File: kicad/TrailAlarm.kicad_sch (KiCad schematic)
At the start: 34 parts

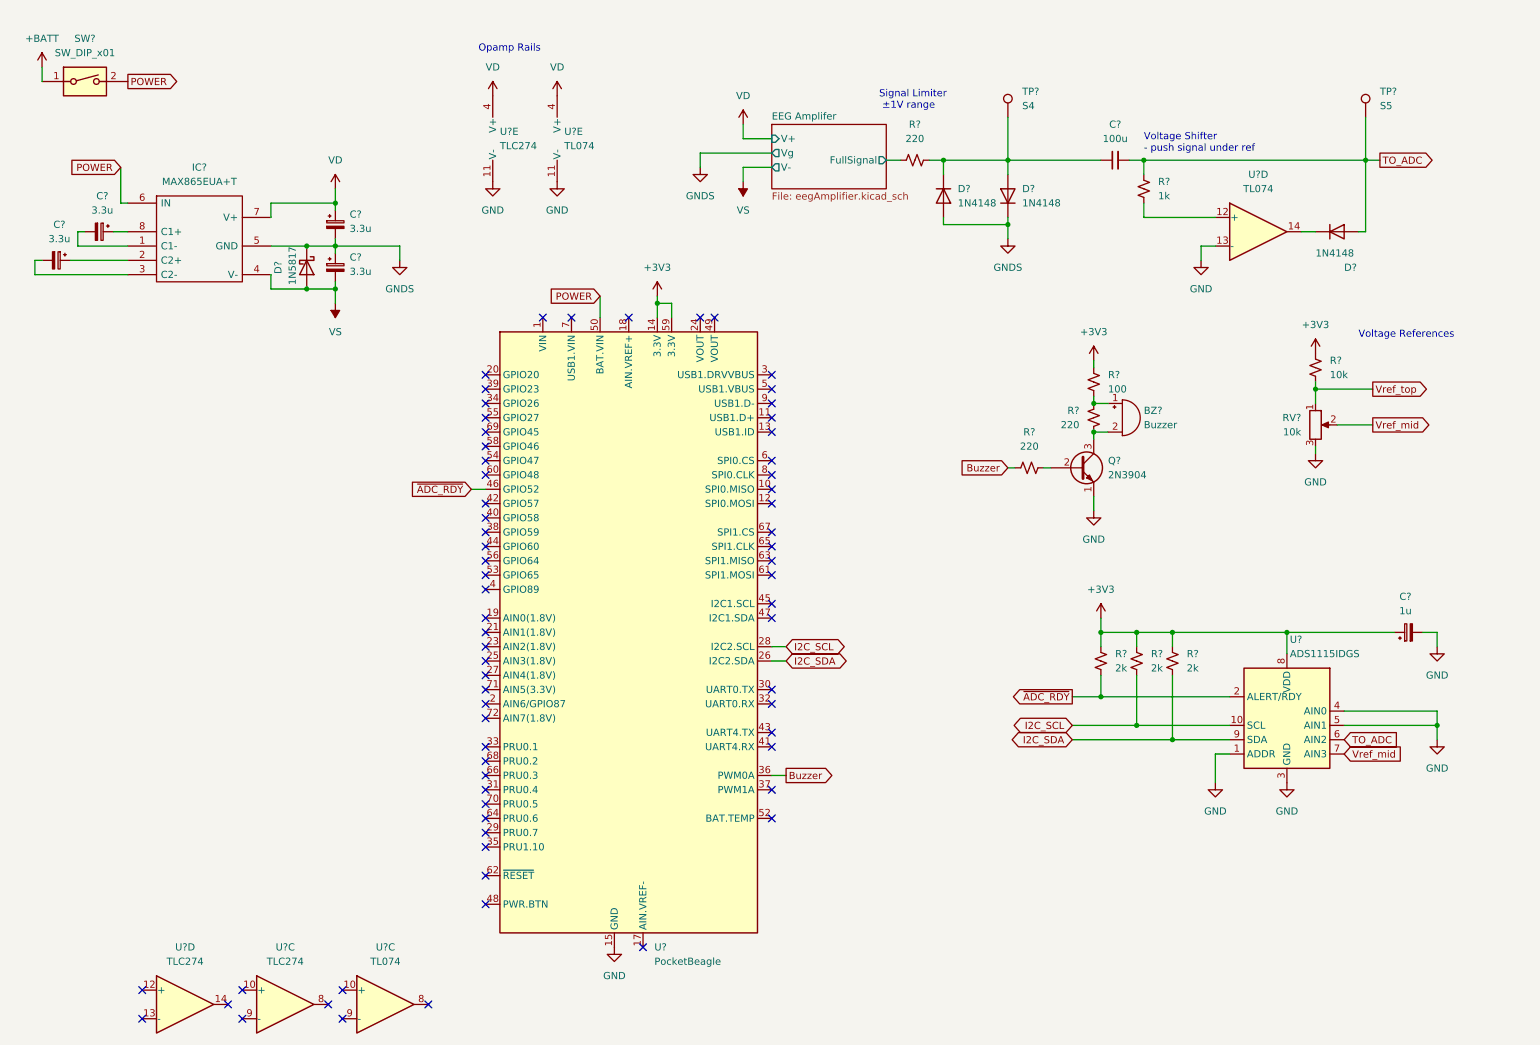
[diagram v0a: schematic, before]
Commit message: Add jumpers to power rails
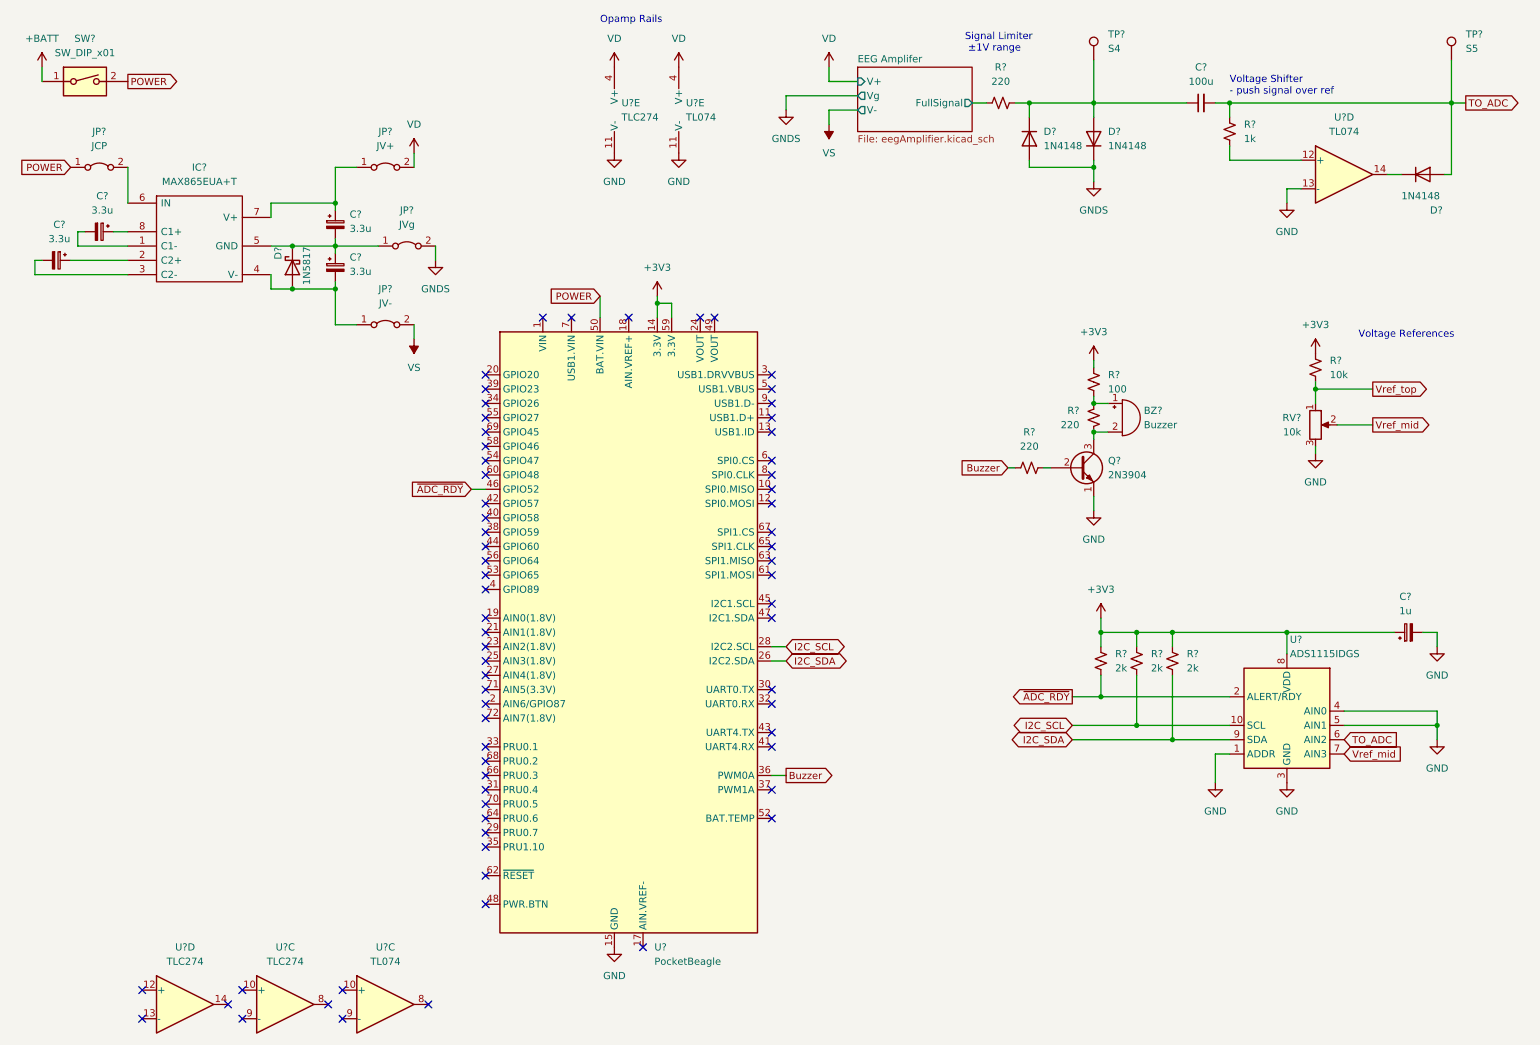
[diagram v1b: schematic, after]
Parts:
- added JP?: JV+, symbol Jumper:Jumper_2_Bridged
- added JP?: JCP, symbol Jumper:Jumper_2_Bridged
- added JP?: JVg, symbol Jumper:Jumper_2_Bridged
- added JP?: JV-, symbol Jumper:Jumper_2_Bridged
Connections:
- net GNDS: now also JP?.2 (B); no longer C?.1, C?.2, D?.1 (K), IC?.5 (GND)
- net POWER: now also JP?.1 (A); no longer IC?.6 (IN)
- net VD: now also JP?.2 (B); no longer C?.1, IC?.7 (V+)
- net VS: now also JP?.2 (B); no longer C?.2, D?.2 (A), IC?.4 (V-)
- new net: C?.1, C?.2, D?.1 (K), IC?.5 (GND), JP?.1 (A)
- new net: C?.2, D?.2 (A), IC?.4 (V-), JP?.1 (A)
- new net: C?.1, IC?.7 (V+), JP?.1 (A)
- new net: IC?.6 (IN), JP?.2 (B)
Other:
- note added: "Voltage Shifter - push signal over ref"
- note removed: "Voltage Shifter - push signal under ref"
- moved on the sheet: C?, D?, R?, TP?, U?D, U?E

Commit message: Pin assignment, electrode headers
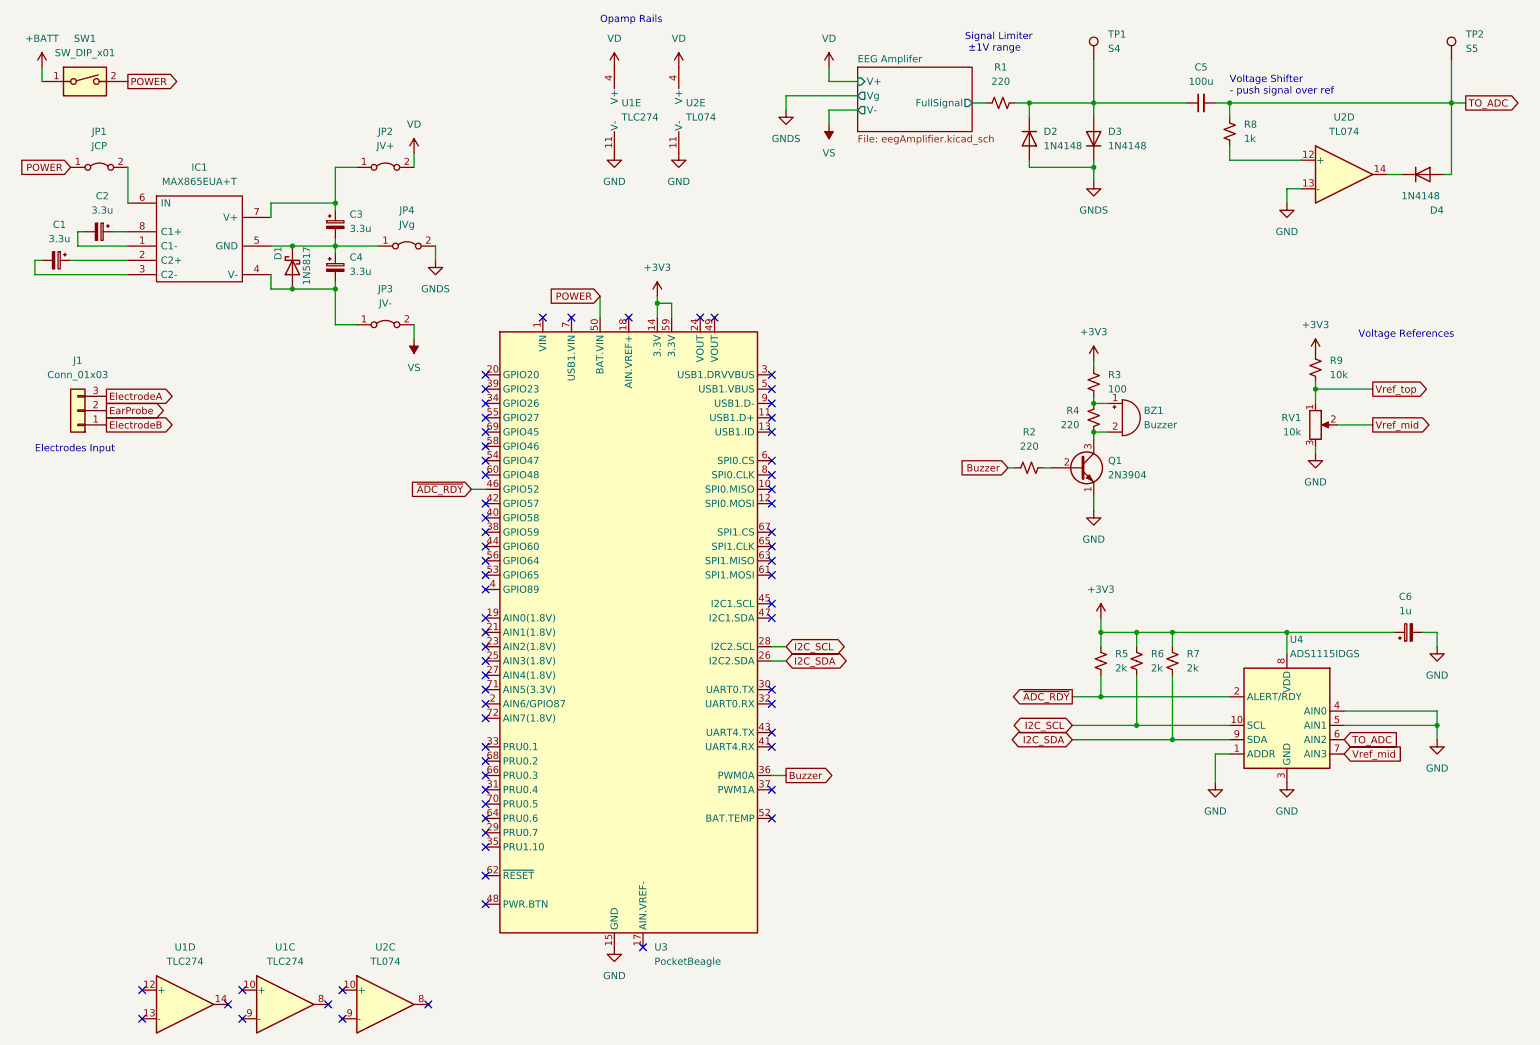
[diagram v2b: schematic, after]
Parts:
- added J1: Conn_01x03, Connector_PinHeader_2.54mm:PinHeader_1x03_P2.54mm_Horizontal, symbol Connector_Generic:Conn_01x03
- gave numbers to parts that had none: 34
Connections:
- new net EarProbe: J1.2 (Pin_2)
- new net ElectrodeA: J1.3 (Pin_3)
- new net ElectrodeB: J1.1 (Pin_1)
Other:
- note added: "Electrodes Input"

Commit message: Done footprint assignment
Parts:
- C1, C2, C3, C4, C6: footprint (none) -> Capacitor_THT:CP_Radial_D4.0mm_P1.50mm
- C5: footprint (none) -> Capacitor_THT:C_Radial_D5.0mm_H7.0mm_P2.00mm
- IC1: footprint SOP65P490X111-8N -> SamacSys:SOP65P490X111-8N
- JP1, JP2, JP3, JP4: footprint (none) -> TestPoint:TestPoint_2Pads_Pitch2.54mm_Drill0.8mm
- R1, R2, R3, R4, R5, R6, R7, R8, R9: footprint (none) -> Resistor_SMD:R_1206_3216Metric_Pad1.30x1.75mm_HandSolder
- TP1, TP2: footprint (none) -> TestPoint:TestPoint_Pad_D1.0mm
- U1, U2: footprint (none) -> Package_DIP:DIP-14_W7.62mm_LongPads
